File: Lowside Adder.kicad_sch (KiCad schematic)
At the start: 6 parts, among them U4 VNL5090, U5 VNL5090, U6 VNL5090, U7 VNL5090

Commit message: All fixed up for JLC
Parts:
- U10: renamed from U5; LCSC (none) -> C2680415
- U11: renamed from U6; LCSC (none) -> C2680415
- U12: renamed from U7; LCSC (none) -> C2680415
- U9: renamed from U4; LCSC (none) -> C2680415
- renumbered RN1 to RN3, RN2 to RN4
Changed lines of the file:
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@@
   (symbol (lib_id "Simon:VNL5090") (at 135.9845 65.1359 0)
     (in_bom yes) (on_board yes) (fields_autoplaced)
-    (property "Reference" "U5" (id 0) (at 135.9845 57.2512 0))
+    (property "Reference" "U10" (id 0) (at 135.9845 57.2512 0))
     (property "Value" "VNL5090" (id 1) (at 135.9845 60.0263 0))
     (property "Footprint" "Package_TO_SOT_SMD:SOT-223" (id 2) (at 135.9845 62.8014 0))
@@
       (effects (font (size 1.27 1.27)) hide)
     )
+    (property "LCSC" "C2680415" (id 4) (at 135.9845 65.1359 0)
+      (effects (font (size 1.27 1.27)) hide)
+    )
     (pin "1")
     (pin "2")
@@
   (symbol (lib_id "Simon:VNL5090") (at 137.101 92.7999 0)
     (in_bom yes) (on_board yes) (fields_autoplaced)
-    (property "Reference" "U7" (id 0) (at 137.101 84.9152 0))
+    (property "Reference" "U12" (id 0) (at 137.101 84.9152 0))
     (property "Value" "VNL5090" (id 1) (at 137.101 87.6903 0))
     (property "Footprint" "Package_TO_SOT_SMD:SOT-223" (id 2) (at 137.101 90.4654 0))
@@
       (effects (font (size 1.27 1.27)) hide)
     )
+    (property "LCSC" "C2680415" (id 4) (at 137.101 92.7999 0)
+      (effects (font (size 1.27 1.27)) hide)
+    )
     (pin "1")
     (pin "2")
@@
   (symbol (lib_id "Device:R_Pack04") (at 109.22 83.82 270) (mirror x)
     (in_bom yes) (on_board yes)
-    (property "Reference" "RN2" (id 0) (at 109.22 94.4118 90))
+    (property "Reference" "RN4" (id 0) (at 109.22 94.4118 90))
     (property "Value" "1k" (id 1) (at 109.22 92.1004 90))
     (property "Footprint" "Resistor_SMD:R_Array_Convex_4x0603" (id 2) (at 109.22 76.835 90)
@@
   (symbol (lib_id "Simon:VNL5090") (at 134.62 50.8 0)
     (in_bom yes) (on_board yes) (fields_autoplaced)
-    (property "Reference" "U4" (id 0) (at 134.62 42.9153 0))
+    (property "Reference" "U9" (id 0) (at 134.62 42.9153 0))
     (property "Value" "VNL5090" (id 1) (at 134.62 45.6904 0))
     (property "Footprint" "Package_TO_SOT_SMD:SOT-223" (id 2) (at 134.62 48.4655 0))
@@
       (effects (font (size 1.27 1.27)) hide)
     )
+    (property "LCSC" "C2680415" (id 4) (at 134.62 50.8 0)
+      (effects (font (size 1.27 1.27)) hide)
+    )
     (pin "1")
     (pin "2")
@@
   (symbol (lib_id "Simon:VNL5090") (at 136.3567 107.1901 0)
     (in_bom yes) (on_board yes) (fields_autoplaced)
-    (property "Reference" "U6" (id 0) (at 136.3567 99.3054 0))
+    (property "Reference" "U11" (id 0) (at 136.3567 99.3054 0))
     (property "Value" "VNL5090" (id 1) (at 136.3567 102.0805 0))
     (property "Footprint" "Package_TO_SOT_SMD:SOT-223" (id 2) (at 136.3567 104.8556 0))
@@
       (effects (font (size 1.27 1.27)) hide)
     )
+    (property "LCSC" "C2680415" (id 4) (at 136.3567 107.1901 0)
+      (effects (font (size 1.27 1.27)) hide)
+    )
     (pin "1")
     (pin "2")
@@
   (symbol (lib_id "Device:R_Pack04") (at 99.06 96.52 0)
     (in_bom yes) (on_board yes)
-    (property "Reference" "RN1" (id 0) (at 88.4682 96.52 90))
+    (property "Reference" "RN3" (id 0) (at 88.4682 96.52 90))
     (property "Value" "1k" (id 1) (at 90.7796 96.52 90))
     (property "Footprint" "Resistor_SMD:R_Array_Convex_4x0603" (id 2) (at 106.045 96.52 90)

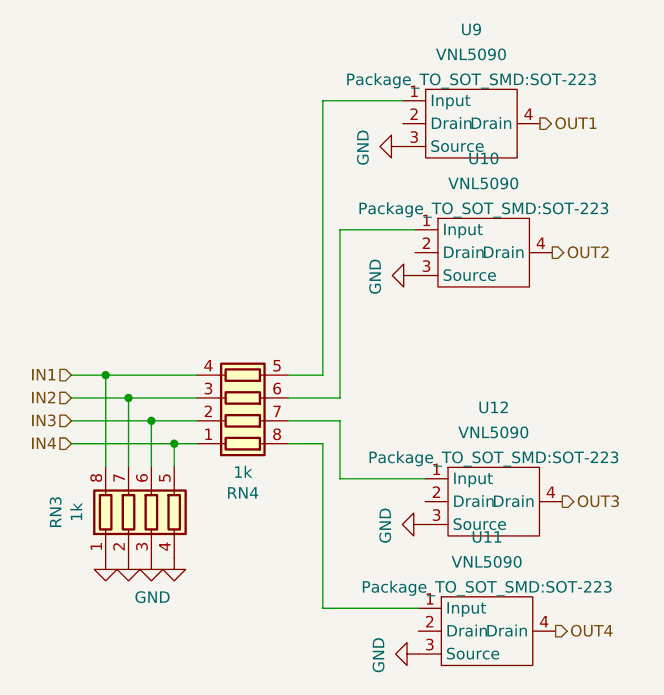
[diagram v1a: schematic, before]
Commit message: Fixed 12V_RAW and added grounds for sensors
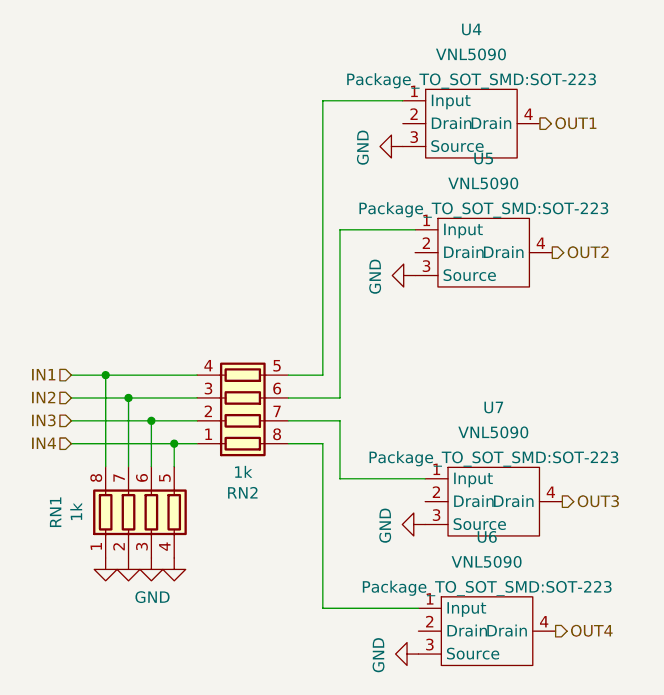
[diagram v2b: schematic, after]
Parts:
- renumbered RN3 to RN1, RN4 to RN2, U9 to U4, U10 to U5, U11 to U6, U12 to U7
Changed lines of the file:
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@@
   (symbol (lib_id "Simon:VNL5090") (at 135.9845 65.1359 0)
     (in_bom yes) (on_board yes) (fields_autoplaced)
-    (property "Reference" "U10" (id 0) (at 135.9845 57.2512 0))
+    (property "Reference" "U5" (id 0) (at 135.9845 57.2512 0))
     (property "Value" "VNL5090" (id 1) (at 135.9845 60.0263 0))
     (property "Footprint" "Package_TO_SOT_SMD:SOT-223" (id 2) (at 135.9845 62.8014 0))
@@
   (symbol (lib_id "power:GND") (at 127 55.88 270)
     (in_bom yes) (on_board yes)
-    (property "Reference" "#PWR058" (id 0) (at 120.65 55.88 0)
+    (property "Reference" "#PWR045" (id 0) (at 120.65 55.88 0)
       (effects (font (size 1.27 1.27)) hide)
     )
@@
   (symbol (lib_id "Simon:VNL5090") (at 137.101 92.7999 0)
     (in_bom yes) (on_board yes) (fields_autoplaced)
-    (property "Reference" "U12" (id 0) (at 137.101 84.9152 0))
+    (property "Reference" "U7" (id 0) (at 137.101 84.9152 0))
     (property "Value" "VNL5090" (id 1) (at 137.101 87.6903 0))
     (property "Footprint" "Package_TO_SOT_SMD:SOT-223" (id 2) (at 137.101 90.4654 0))
@@
   (symbol (lib_id "power:GND") (at 93.98 101.6 0)
     (in_bom yes) (on_board yes)
-    (property "Reference" "#PWR054" (id 0) (at 93.98 107.95 0)
+    (property "Reference" "#PWR041" (id 0) (at 93.98 107.95 0)
       (effects (font (size 1.27 1.27)) hide)
     )
@@
   (symbol (lib_id "power:GND") (at 129.481 97.8799 270)
     (in_bom yes) (on_board yes)
-    (property "Reference" "#PWR061" (id 0) (at 123.131 97.8799 0)
+    (property "Reference" "#PWR048" (id 0) (at 123.131 97.8799 0)
       (effects (font (size 1.27 1.27)) hide)
     )
@@
   (symbol (lib_id "power:GND") (at 96.52 101.6 0)
     (in_bom yes) (on_board yes)
-    (property "Reference" "#PWR055" (id 0) (at 96.52 107.95 0)
+    (property "Reference" "#PWR042" (id 0) (at 96.52 107.95 0)
       (effects (font (size 1.27 1.27)) hide)
     )
@@
   (symbol (lib_id "power:GND") (at 101.6 101.6 0)
     (in_bom yes) (on_board yes)
-    (property "Reference" "#PWR057" (id 0) (at 101.6 107.95 0)
+    (property "Reference" "#PWR044" (id 0) (at 101.6 107.95 0)
       (effects (font (size 1.27 1.27)) hide)
     )
@@
   (symbol (lib_id "power:GND") (at 128.7367 112.2701 270)
     (in_bom yes) (on_board yes)
-    (property "Reference" "#PWR060" (id 0) (at 122.3867 112.2701 0)
+    (property "Reference" "#PWR047" (id 0) (at 122.3867 112.2701 0)
       (effects (font (size 1.27 1.27)) hide)
     )
@@
   (symbol (lib_id "power:GND") (at 99.06 101.6 0)
     (in_bom yes) (on_board yes)
-    (property "Reference" "#PWR056" (id 0) (at 99.06 107.95 0)
+    (property "Reference" "#PWR043" (id 0) (at 99.06 107.95 0)
       (effects (font (size 1.27 1.27)) hide)
     )
@@
   (symbol (lib_id "power:GND") (at 128.3645 70.2159 270)
     (in_bom yes) (on_board yes)
-    (property "Reference" "#PWR059" (id 0) (at 122.0145 70.2159 0)
+    (property "Reference" "#PWR046" (id 0) (at 122.0145 70.2159 0)
       (effects (font (size 1.27 1.27)) hide)
     )
@@
   (symbol (lib_id "Device:R_Pack04") (at 109.22 83.82 270) (mirror x)
     (in_bom yes) (on_board yes)
-    (property "Reference" "RN4" (id 0) (at 109.22 94.4118 90))
+    (property "Reference" "RN2" (id 0) (at 109.22 94.4118 90))
     (property "Value" "1k" (id 1) (at 109.22 92.1004 90))
     (property "Footprint" "Resistor_SMD:R_Array_Convex_4x0603" (id 2) (at 109.22 76.835 90)
@@
   (symbol (lib_id "Simon:VNL5090") (at 134.62 50.8 0)
     (in_bom yes) (on_board yes) (fields_autoplaced)
-    (property "Reference" "U9" (id 0) (at 134.62 42.9153 0))
+    (property "Reference" "U4" (id 0) (at 134.62 42.9153 0))
     (property "Value" "VNL5090" (id 1) (at 134.62 45.6904 0))
     (property "Footprint" "Package_TO_SOT_SMD:SOT-223" (id 2) (at 134.62 48.4655 0))
@@
   (symbol (lib_id "Simon:VNL5090") (at 136.3567 107.1901 0)
     (in_bom yes) (on_board yes) (fields_autoplaced)
-    (property "Reference" "U11" (id 0) (at 136.3567 99.3054 0))
+    (property "Reference" "U6" (id 0) (at 136.3567 99.3054 0))
     (property "Value" "VNL5090" (id 1) (at 136.3567 102.0805 0))
     (property "Footprint" "Package_TO_SOT_SMD:SOT-223" (id 2) (at 136.3567 104.8556 0))
@@
   (symbol (lib_id "Device:R_Pack04") (at 99.06 96.52 0)
     (in_bom yes) (on_board yes)
-    (property "Reference" "RN3" (id 0) (at 88.4682 96.52 90))
+    (property "Reference" "RN1" (id 0) (at 88.4682 96.52 90))
     (property "Value" "1k" (id 1) (at 90.7796 96.52 90))
     (property "Footprint" "Resistor_SMD:R_Array_Convex_4x0603" (id 2) (at 106.045 96.52 90)
